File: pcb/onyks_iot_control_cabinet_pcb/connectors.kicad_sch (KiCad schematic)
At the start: 5 parts, among them J5 Conn_01x07_Socket, J6 Conn_01x04_Socket, J7 Screw_Terminal_01x02, J8 Conn_01x04_Socket, J9 Conn_01x02_Socket

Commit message: Assignment some footprints to symbols
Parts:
- J5: footprint (none) -> Connector_PinHeader_2.54mm:PinHeader_1x07_P2.54mm_Vertical
- J6, J8: footprint (none) -> Connector_PinHeader_2.54mm:PinHeader_1x04_P2.54mm_Vertical
- J7: footprint (none) -> TerminalBlock:TerminalBlock_Xinya_XY308-2.54-2P_1x02_P2.54mm_Horizontal
- J9: footprint (none) -> Connector_PinHeader_2.54mm:PinHeader_1x02_P2.54mm_Vertical
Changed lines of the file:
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@@
 			)
 		)
-		(property "Footprint" ""
+		(property "Footprint" "Connector_PinHeader_2.54mm:PinHeader_1x04_P2.54mm_Vertical"
 			(at 49.53 74.93 0)
 			(effects
@@
 			)
 		)
-		(property "Footprint" ""
+		(property "Footprint" "Connector_PinHeader_2.54mm:PinHeader_1x07_P2.54mm_Vertical"
 			(at 41.91 138.43 0)
 			(effects
@@
 			)
 		)
-		(property "Footprint" ""
+		(property "Footprint" "TerminalBlock:TerminalBlock_Xinya_XY308-2.54-2P_1x02_P2.54mm_Horizontal"
 			(at 49.53 34.29 0)
 			(effects
@@
 			)
 		)
-		(property "Footprint" ""
+		(property "Footprint" "Connector_PinHeader_2.54mm:PinHeader_1x04_P2.54mm_Vertical"
 			(at 44.45 107.95 0)
 			(effects
@@
 			)
 		)
-		(property "Footprint" ""
+		(property "Footprint" "Connector_PinHeader_2.54mm:PinHeader_1x02_P2.54mm_Vertical"
 			(at 50.8 43.18 0)
 			(effects

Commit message: PCB - Finished, needs additional confirmation
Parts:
- removed J5: Conn_01x07_Socket, Connector_PinHeader_2.54mm:PinHeader_1x07_P2.54mm_Vertical, symbol Connector:Conn_01x07_Socket
- added J5: Conn_01x09_Socket, Connector_PinHeader_2.54mm:PinHeader_1x09_P2.54mm_Vertical, symbol Connector:Conn_01x09_Socket
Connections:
- net GPIO_1: now also J5.1 (Pin_1)
- net GPIO_2: now also J5.2 (Pin_2)
- net GPIO_3: now also J5.3 (Pin_3)
- net GPIO_4: now also J5.4 (Pin_4)
- net GPIO_5: now also J5.5 (Pin_5)
- net GPIO_6: now also J5.6 (Pin_6)
- net GPIO_7: now also J5.7 (Pin_7)
- new net GPIO_8: J5.8 (Pin_8)
- new net GPIO_9: J5.9 (Pin_9)
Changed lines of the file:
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@@
+	(wire
+		(pts
+			(xy 31.75 151.13) (xy 36.83 151.13)
+		)
+		(stroke
+			(width 0)
+			(type default)
+		)
+	)
 	(wire
 		(pts
@@
 		(pts
 			(xy 44.45 74.93) (xy 35.56 74.93)
+		)
+		(stroke
+			(width 0)
+			(type default)
+		)
+	)
+	(wire
+		(pts
+			(xy 31.75 148.59) (xy 36.83 148.59)
 		)
 		(stroke
@@
 	(rectangle
 		(start 19.05 121.92)
-		(end 81.28 148.59)
+		(end 81.28 153.67)
 		(stroke
 			(width 0.635)
@@
 		)
 	)
+	(hierarchical_label "GPIO_9"
+		(shape input)
+		(at 31.75 151.13 180)
+		(fields_autoplaced yes)
+		(effects
+			(font
+				(size 1.27 1.27)
+			)
+			(justify right)
+		)
+	)
 	(hierarchical_label "DTR"
 		(shape input)
@@
 		)
 	)
+	(hierarchical_label "GPIO_8"
+		(shape input)
+		(at 31.75 148.59 180)
+		(fields_autoplaced yes)
+		(effects
+			(font
+				(size 1.27 1.27)
+			)
+			(justify right)
+		)
+	)
 	(hierarchical_label "LOCK_N"
 		(shape input)
@@
 			)
 			(justify right)
+		)
+	)
+	(symbol
+		(lib_id "Connector:Conn_01x09_Socket")
+		(at 41.91 140.97 0)
+		(unit 1)
+		(exclude_from_sim no)
+		(in_bom yes)
+		(on_board yes)
+		(dnp no)
+		(fields_autoplaced yes)
+		(property "Reference" "J5"
+			(at 43.18 139.6999 0)
+			(effects
+				(font
+					(size 1.27 1.27)
+				)
+				(justify left)
+			)
+		)
+		(property "Value" "Conn_01x09_Socket"
+			(at 43.18 142.2399 0)
+			(effects
+				(font
+					(size 1.27 1.27)
+				)
+				(justify left)
+			)
+		)
+		(property "Footprint" "Connector_PinHeader_2.54mm:PinHeader_1x09_P2.54mm_Vertical"
+			(at 41.91 140.97 0)
+			(effects
+				(font
+					(size 1.27 1.27)
+				)
+				(hide yes)
+			)
+		)
+		(property "Datasheet" "~"
+			(at 41.91 140.97 0)
+			(effects
+				(font
+					(size 1.27 1.27)
+				)
+				(hide yes)
+			)
+		)
+		(property "Description" "Generic connector, single row, 01x09, script generated"
+			(at 41.91 140.97 0)
+			(effects
+				(font
+					(size 1.27 1.27)
+				)
+				(hide yes)
+			)
+		)
+		(pin "1"
+		)
+		(pin "8"
+		)
+		(pin "5"
+		)
+		(pin "3"
+		)
+		(pin "2"
+		)
+		(pin "4"
+		)
+		(pin "7"
+		)
+		(pin "9"
+		)
+		(pin "6"
+		)
+		(instances
+			(project ""
+				(path "/789878cb-67d5-4bc7-a42d-b3bc72d661d0/9fa608f4-5282-4caa-ae1b-46582b97cb5d"
+					(reference "J5")
+					(unit 1)
+				)
+			)
 		)
 	)
@@
 					(unit 1)
 				)
-			)
-		)
-	)
-	(symbol
-		(lib_id "Connector:Conn_01x07_Socket")
-		(at 41.91 138.43 0)
-		(unit 1)
-		(exclude_from_sim no)
-		(in_bom yes)
-		(on_board yes)
-		(dnp no)
-		(fields_autoplaced yes)
-		(property "Reference" "J5"
-			(at 43.18 137.1599 0)
-			(effects
-				(font
-					(size 1.27 1.27)
-				)
-				(justify left)
-			)
-		)
-		(property "Value" "Conn_01x07_Socket"
-			(at 43.18 139.6999 0)
-			(effects
-				(font
-					(size 1.27 1.27)
-				)
-				(justify left)
-			)
-		)
-		(property "Footprint" "Connector_PinHeader_2.54mm:PinHeader_1x07_P2.54mm_Vertical"
-			(at 41.91 138.43 0)
-			(effects
-				(font
-					(size 1.27 1.27)
-				)
-				(hide yes)
-			)
-		)
-		(property "Datasheet" "~"
-			(at 41.91 138.43 0)
-			(effects
-				(font
-					(size 1.27 1.27)
-				)
-				(hide yes)
-			)
-		)
-		(property "Description" "Generic connector, single row, 01x07, script generated"
-			(at 41.91 138.43 0)
-			(effects
-				(font
-					(size 1.27 1.27)
-				)
-				(hide yes)
-			)
-		)
-		(pin "4"
-		)
-		(pin "3"
-		)
-		(pin "2"
-		)
-		(pin "6"
-		)
-		(pin "5"
-		)
-		(pin "1"
-		)
-		(pin "7"
-		)
-		(instances
-			(project "onyks_iot_control_cabinet_pcb"
-				(path "/789878cb-67d5-4bc7-a42d-b3bc72d661d0/9fa608f4-5282-4caa-ae1b-46582b97cb5d"
-					(reference "J5")
-					(unit 1)
-				)

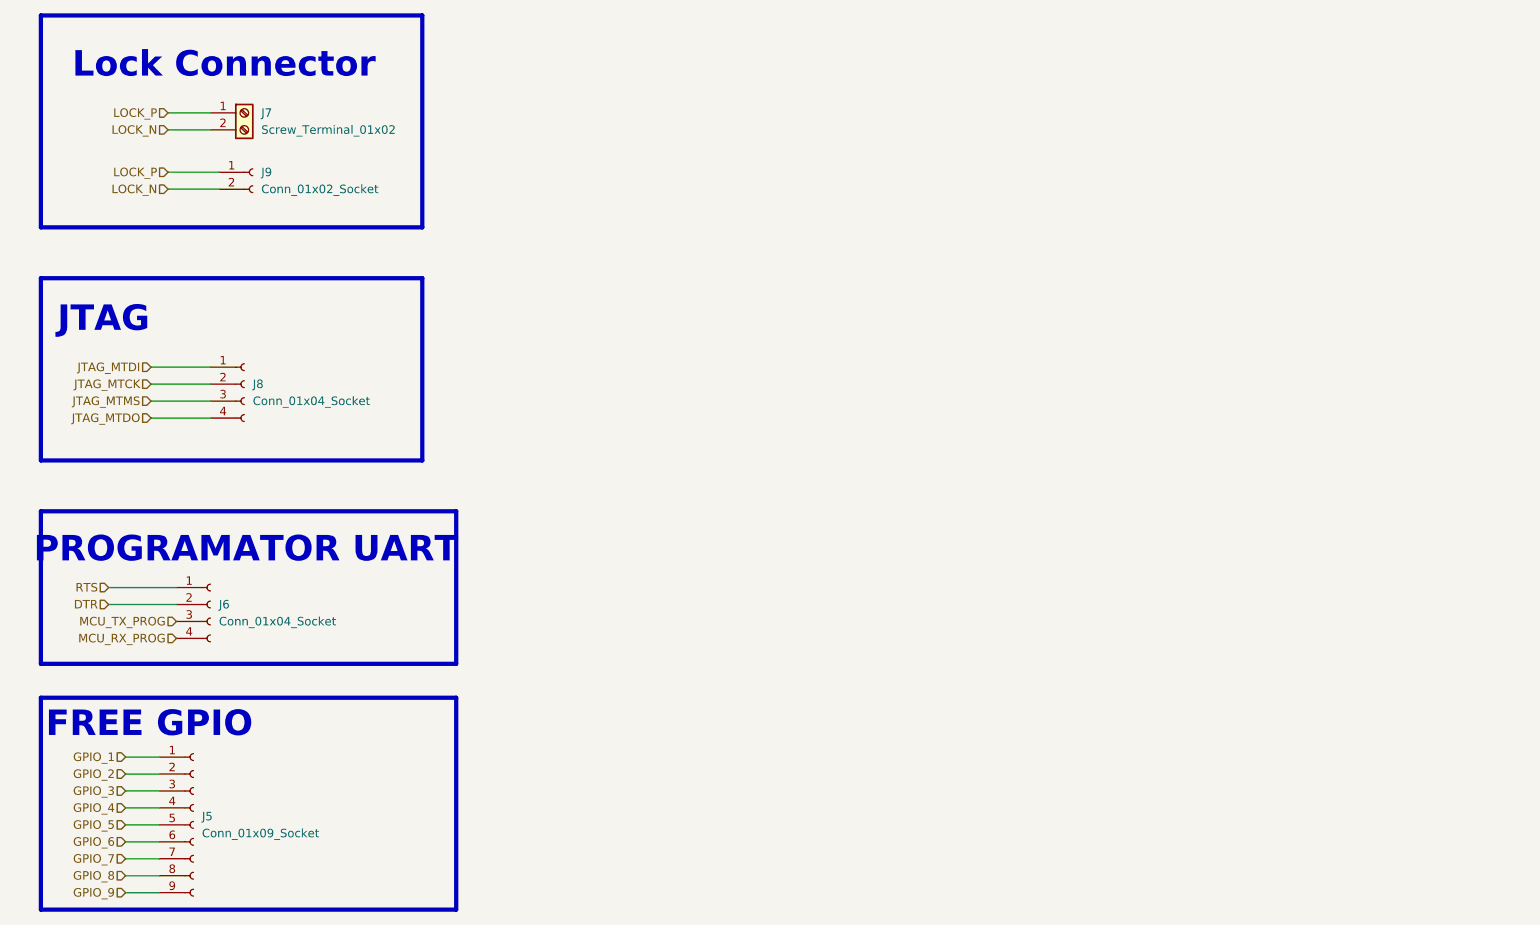
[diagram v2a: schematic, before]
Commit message: Change some elements footprints
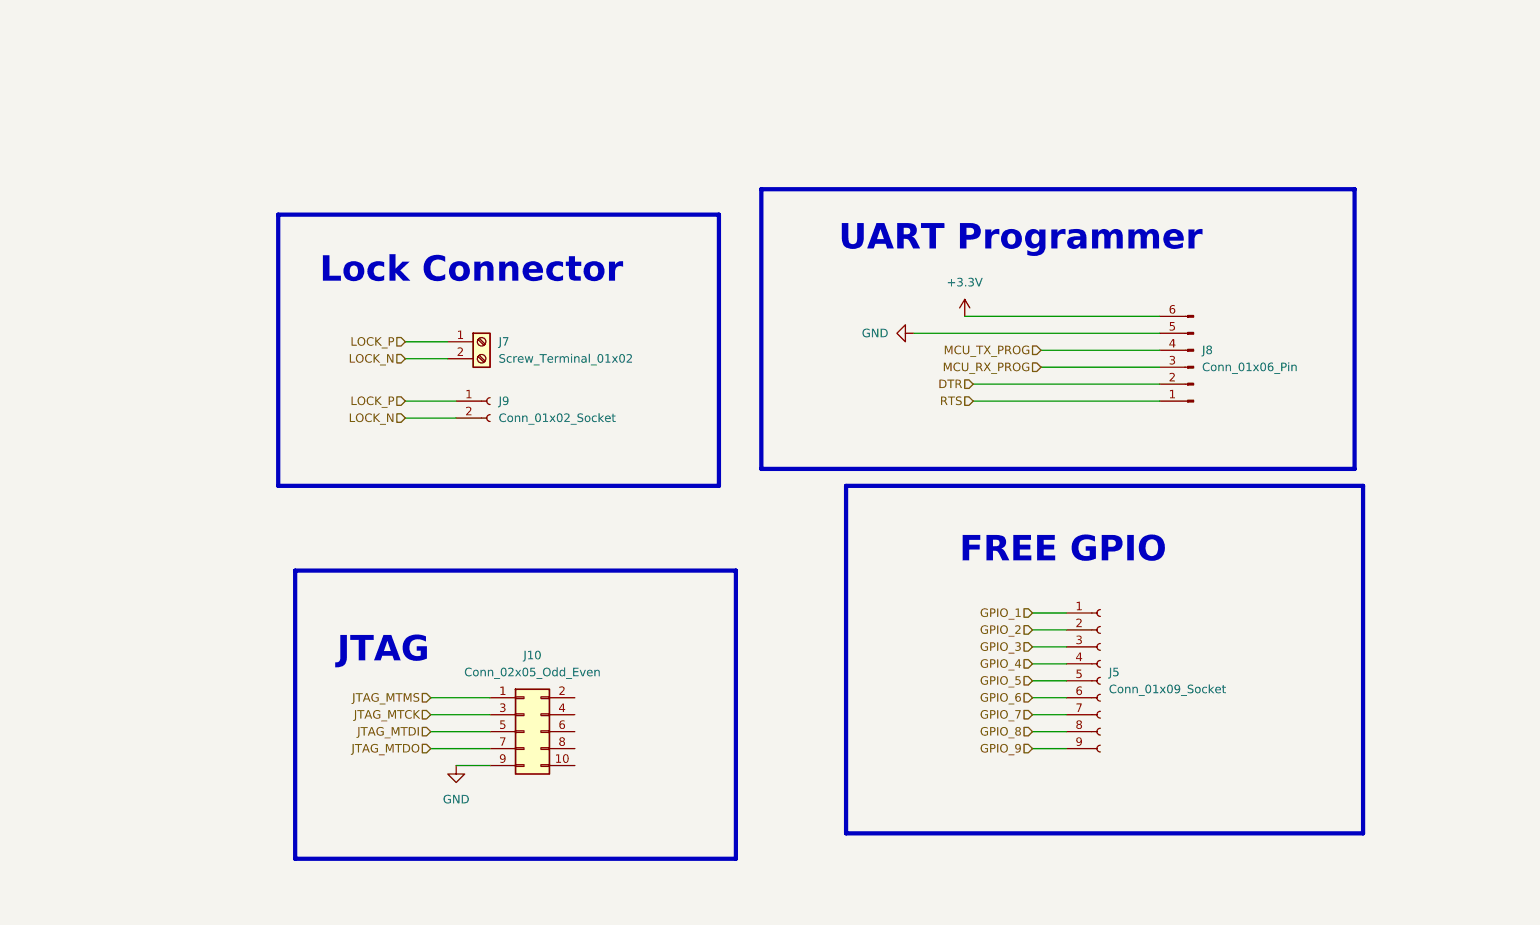
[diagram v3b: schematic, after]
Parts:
- removed J6, J8: Conn_01x04_Socket, Connector_PinHeader_2.54mm:PinHeader_1x04_P2.54mm_Vertical, symbol Connector:Conn_01x04_Socket
- added J10: Conn_02x05_Odd_Even, Connector_PinHeader_2.54mm:PinHeader_2x05_P2.54mm_Vertical, symbol Connector_Generic:Conn_02x05_Odd_Even
- added J8: Conn_01x06_Pin, Connector_PinHeader_2.54mm:PinHeader_1x06_P2.54mm_Vertical, symbol Connector:Conn_01x06_Pin
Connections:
- net DTR: now also J8.2 (Pin_2)
- net JTAG_MTCK: now also J10.3 (Pin_3)
- net JTAG_MTDI: now also J10.5 (Pin_5)
- net JTAG_MTDO: now also J10.7 (Pin_7)
- net JTAG_MTMS: now also J10.1 (Pin_1)
- net MCU_RX_PROG: now also J8.3 (Pin_3)
- net MCU_TX_PROG: now also J8.4 (Pin_4)
- net RTS: now also J8.1 (Pin_1)
- new net +3.3V: J8.6 (Pin_6)
- new net GND: J10.9 (Pin_9), J8.5 (Pin_5)
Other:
- note added: "UART Programmer"
- note removed: "PROGRAMATOR UART"
- moved on the sheet: J5, J7, J9

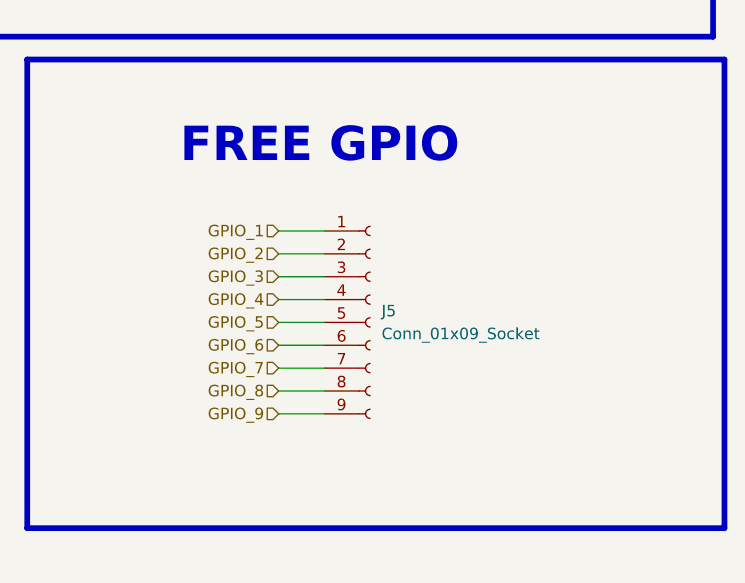
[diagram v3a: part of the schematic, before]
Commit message: Change the connector of GPIOs
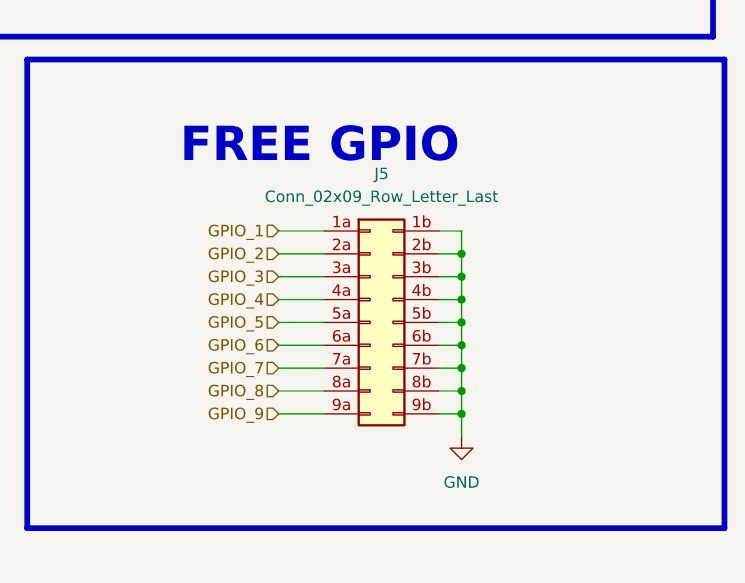
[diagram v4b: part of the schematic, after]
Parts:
- removed J5: Conn_01x09_Socket, Connector_PinHeader_2.54mm:PinHeader_1x09_P2.54mm_Vertical, symbol Connector:Conn_01x09_Socket
- added J5: Conn_02x09_Row_Letter_Last, Connector_PinSocket_2.54mm:PinSocket_2x09_P2.54mm_Vertical, symbol Connector_Generic:Conn_02x09_Row_Letter_Last
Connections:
- net GND: now also J5.1b (Pin_1b), J5.2b (Pin_2b), J5.3b (Pin_3b), J5.4b (Pin_4b), J5.5b (Pin_5b), J5.6b (Pin_6b), J5.7b (Pin_7b), J5.8b (Pin_8b), J5.9b (Pin_9b)
- net GPIO_1: now also J5.1a (Pin_1a)
- net GPIO_2: now also J5.2a (Pin_2a)
- net GPIO_3: now also J5.3a (Pin_3a)
- net GPIO_4: now also J5.4a (Pin_4a)
- net GPIO_5: now also J5.5a (Pin_5a)
- net GPIO_6: now also J5.6a (Pin_6a)
- net GPIO_7: now also J5.7a (Pin_7a)
- net GPIO_8: now also J5.8a (Pin_8a)
- net GPIO_9: now also J5.9a (Pin_9a)

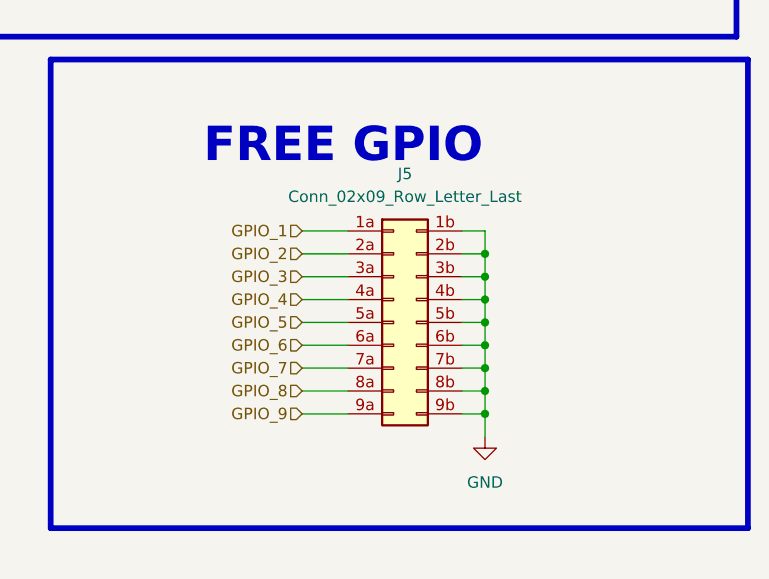
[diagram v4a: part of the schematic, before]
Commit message: Patching GND for Free GPIO Connections
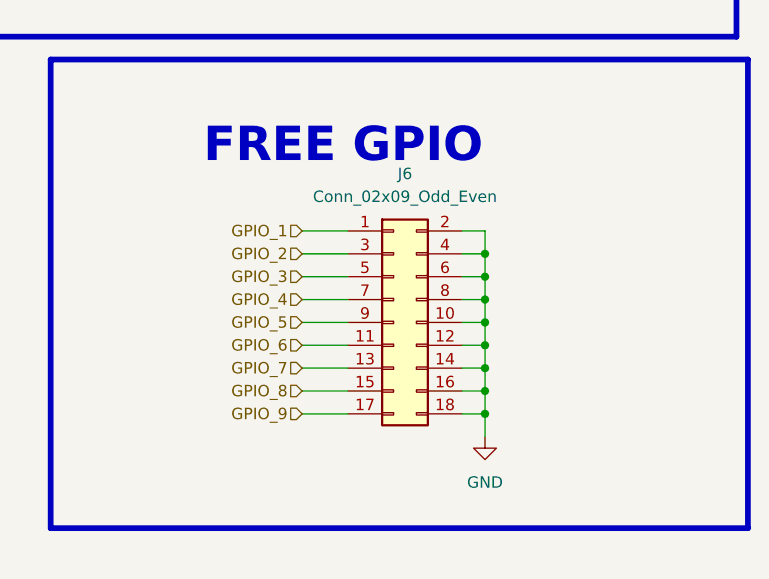
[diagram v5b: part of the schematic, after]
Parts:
- removed J5: Conn_02x09_Row_Letter_Last, Connector_PinSocket_2.54mm:PinSocket_2x09_P2.54mm_Vertical, symbol Connector_Generic:Conn_02x09_Row_Letter_Last
- added J6: Conn_02x09_Odd_Even, Connector_PinHeader_2.54mm:PinHeader_2x09_P2.54mm_Vertical, symbol Connector_Generic:Conn_02x09_Odd_Even
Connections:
- net GND: now also J6.10 (Pin_10), J6.12 (Pin_12), J6.14 (Pin_14), J6.16 (Pin_16), J6.18 (Pin_18), J6.2 (Pin_2), J6.4 (Pin_4), J6.6 (Pin_6), J6.8 (Pin_8)
- net GPIO_1: now also J6.1 (Pin_1)
- net GPIO_2: now also J6.3 (Pin_3)
- net GPIO_3: now also J6.5 (Pin_5)
- net GPIO_4: now also J6.7 (Pin_7)
- net GPIO_5: now also J6.9 (Pin_9)
- net GPIO_6: now also J6.11 (Pin_11)
- net GPIO_7: now also J6.13 (Pin_13)
- net GPIO_8: now also J6.15 (Pin_15)
- net GPIO_9: now also J6.17 (Pin_17)

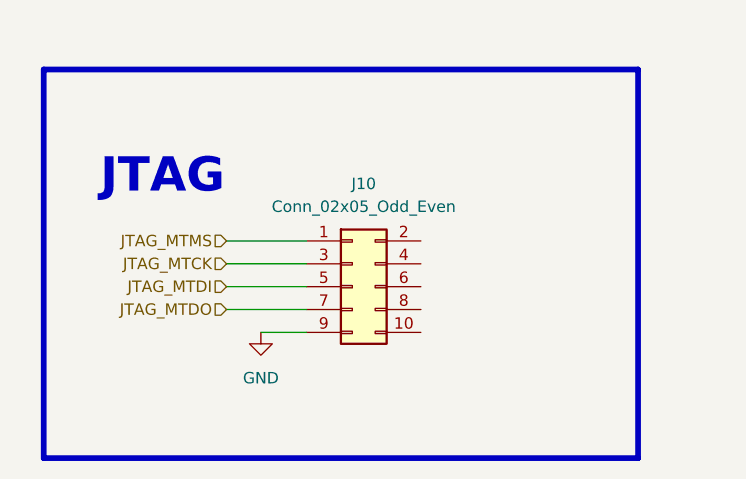
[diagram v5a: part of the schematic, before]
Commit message: Add new rules, change JTAG and VCC polygon plane
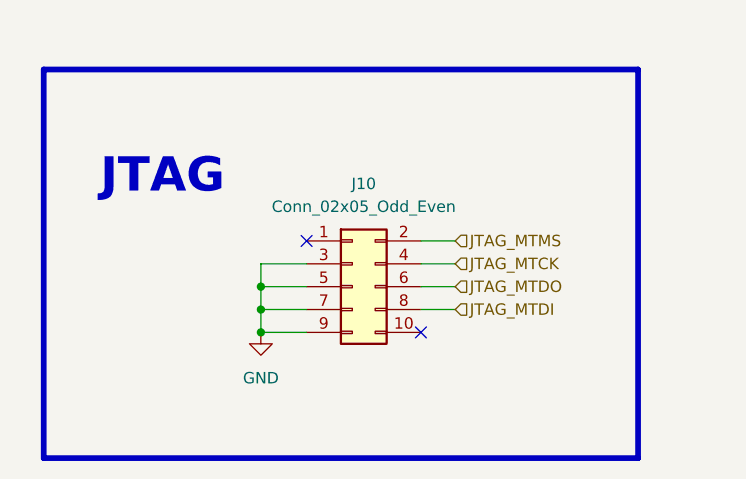
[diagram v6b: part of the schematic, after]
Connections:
- net GND: now also J10.3 (Pin_3), J10.5 (Pin_5), J10.7 (Pin_7)
- net JTAG_MTCK: now also J10.4 (Pin_4); no longer J10.3 (Pin_3)
- net JTAG_MTDI: now also J10.8 (Pin_8); no longer J10.5 (Pin_5)
- net JTAG_MTDO: now also J10.6 (Pin_6); no longer J10.7 (Pin_7)
- net JTAG_MTMS: now also J10.2 (Pin_2); no longer J10.1 (Pin_1)
- no-connect marks 0 -> 2
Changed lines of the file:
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@@
+	)
+	(junction
+		(at 81.28 127)
+		(diameter 0)
+		(color 0 0 0 0)
+	)
+	(junction
+		(at 81.28 129.54)
+		(diameter 0)
+		(color 0 0 0 0)
 	)
 	(junction
@@
 	)
 	(junction
+		(at 81.28 132.08)
+		(diameter 0)
+		(color 0 0 0 0)
+	)
+	(junction
 		(at 187.96 114.3)
 		(diameter 0)
@@
 		(color 0 0 0 0)
 	)
+	(no_connect
+		(at 86.36 121.92)
+	)
+	(no_connect
+		(at 99.06 132.08)
+	)
 	(wire
 		(pts
@@
 	(wire
 		(pts
+			(xy 81.28 127) (xy 81.28 129.54)
+		)
+		(stroke
+			(width 0)
+			(type default)
+		)
+	)
+	(wire
+		(pts
 			(xy 167.64 119.38) (xy 172.72 119.38)
 		)
@@
 	(wire
 		(pts
-			(xy 86.36 129.54) (xy 77.47 129.54)
-		)
-		(stroke
-			(width 0)
-			(type default)
-		)
-	)
-	(wire
-		(pts
 			(xy 158.75 77.47) (xy 186.69 77.47)
 		)
@@
 	(wire
 		(pts
-			(xy 86.36 127) (xy 77.47 127)
+			(xy 99.06 127) (xy 102.87 127)
 		)
 		(stroke
@@
 	(wire
 		(pts
-			(xy 86.36 124.46) (xy 77.47 124.46)
+			(xy 99.06 121.92) (xy 102.87 121.92)
 		)
 		(stroke
@@
 	(wire
 		(pts
-			(xy 86.36 121.92) (xy 77.47 121.92)
+			(xy 99.06 124.46) (xy 102.87 124.46)
+		)
+		(stroke
+			(width 0)
+			(type default)
+		)
+	)
+	(wire
+		(pts
+			(xy 99.06 129.54) (xy 102.87 129.54)
 		)
 		(stroke
@@
 	(wire
 		(pts
+			(xy 81.28 129.54) (xy 86.36 129.54)
+		)
+		(stroke
+			(width 0)
+			(type default)
+		)
+	)
+	(wire
+		(pts
 			(xy 187.96 119.38) (xy 187.96 121.92)
 		)
@@
 	(wire
 		(pts
+			(xy 81.28 124.46) (xy 81.28 127)
+		)
+		(stroke
+			(width 0)
+			(type default)
+		)
+	)
+	(wire
+		(pts
 			(xy 185.42 127) (xy 187.96 127)
 		)
@@
 	(wire
 		(pts
+			(xy 81.28 129.54) (xy 81.28 132.08)
+		)
+		(stroke
+			(width 0)
+			(type default)
+		)
+	)
+	(wire
+		(pts
 			(xy 167.64 114.3) (xy 172.72 114.3)
+		)
+		(stroke
+			(width 0)
+			(type default)
+		)
+	)
+	(wire
+		(pts
+			(xy 86.36 124.46) (xy 81.28 124.46)
+		)
+		(stroke
+			(width 0)
+			(type default)
+		)
+	)
+	(wire
+		(pts
+			(xy 81.28 127) (xy 86.36 127)
 		)
 		(stroke
@@
 	(hierarchical_label "JTAG_MTMS"
 		(shape input)
-		(at 77.47 121.92 180)
-		(fields_autoplaced yes)
-		(effects
-			(font
-				(size 1.27 1.27)
-			)
-			(justify right)
+		(at 102.87 121.92 0)
+		(fields_autoplaced yes)
+		(effects
+			(font
+				(size 1.27 1.27)
+			)
+			(justify left)
 		)
 	)
@@
 	(hierarchical_label "JTAG_MTCK"
 		(shape input)
-		(at 77.47 124.46 180)
-		(fields_autoplaced yes)
-		(effects
-			(font
-				(size 1.27 1.27)
-			)
-			(justify right)
+		(at 102.87 124.46 0)
+		(fields_autoplaced yes)
+		(effects
+			(font
+				(size 1.27 1.27)
+			)
+			(justify left)
 		)
 	)
 	(hierarchical_label "JTAG_MTDI"
 		(shape input)
-		(at 77.47 127 180)
-		(fields_autoplaced yes)
-		(effects
-			(font
-				(size 1.27 1.27)
-			)
-			(justify right)
+		(at 102.87 129.54 0)
+		(fields_autoplaced yes)
+		(effects
+			(font
+				(size 1.27 1.27)
+			)
+			(justify left)
 		)
 	)
@@
 	(hierarchical_label "JTAG_MTDO"
 		(shape input)
-		(at 77.47 129.54 180)
-		(fields_autoplaced yes)
-		(effects
-			(font
-				(size 1.27 1.27)
-			)
-			(justify right)
-		)
-	)
+		(at 102.87 127 0)
+		(fields_autoplaced yes)
+		(effects
+			(font
+				(size 1.27 1.27)
+			)
+			(justify left)
+		)
+	)
